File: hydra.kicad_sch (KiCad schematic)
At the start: 59 parts, among them J1 PC104 Interconnect, J2 STLINK/V2 Header, J3 STLINK/V2 Clone Header, J4 USB Conn, J5 UART Header, U2 AMS1117-3.3, U3 STM32F103VCTx, Y1 16mHz

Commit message: feat: mostly done pcb
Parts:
- removed D2: Power LED, symbol Device:LED
- removed J4: USB Conn, symbol Connector:USB_C_Receptacle_USB2.0_14P
- removed R2, R3, R4: 5.1k, symbol Device:R
- removed R5: 9k, symbol Device:R
- added C10, C11, C12, C13, C14: 0.1uF, Capacitor_SMD:C_0603_1608Metric, symbol Device:C
- added H1, H2, H3, H4: MountingHole, MountingHole:MountingHole_3.2mm_M3_DIN965_Pad, symbol Mechanical:MountingHole
- C1, C2, C3, C4, C5, C6, C7, C8, C9: footprint (none) -> Capacitor_SMD:C_0603_1608Metric
- D1, D10, D11, D12, D13, D14, D3, D4, D5, D6, D7, D8, D9: footprint (none) -> LED_SMD:LED_0603_1608Metric
- J1: footprint (none) -> Connector_PinHeader_2.54mm:PinHeader_2x32_P2.54mm_Vertical; symbol Connector_Generic_MountingPin:Conn_02x32_Row_Letter_First_MountingPin -> Connector_Generic_MountingPin:Conn_02x32_Odd_Even_MountingPin
- J2: footprint (none) -> Connector_PinHeader_2.54mm:PinHeader_2x10_P2.54mm_Vertical
- J3: footprint (none) -> Connector_PinHeader_2.54mm:PinHeader_2x05_P2.54mm_Vertical
- J5: footprint (none) -> Connector_PinHeader_2.54mm:PinHeader_1x03_P2.54mm_Vertical
- R1: value 4.7k -> 5.1k; footprint (none) -> Resistor_SMD:R_0603_1608Metric
- R10, R11, R12, R13, R14, R15, R16, R6, R7, R8, R9: value 4.7K -> 5.1K; footprint (none) -> Resistor_SMD:R_0603_1608Metric
- R17: value 4.7K -> 5.1K; footprint (none) -> Capacitor_SMD:C_0603_1608Metric
- TP1, TP10, TP11, TP2, TP3, TP4, TP5, TP6, TP7, TP8, TP9: footprint (none) -> TestPoint:TestPoint_Pad_D1.0mm
- Y1: footprint (none) -> Crystal:Crystal_HC49-U_Vertical
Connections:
- net +3V3: now also C10.1, C11.1, C12.1, C13.1, C14.1
- net 3V3_CONN: now also J1.57 (Pin_57), J1.58 (Pin_58); no longer J1.a29 (Pin_a29), J1.b29 (Pin_b29)
- net CS_1: now also J1.1 (Pin_1), J1.2 (Pin_2), U3.67 (PA8); no longer J1.a1 (Pin_a1), J1.b1 (Pin_b1), U3.15 (PC0)
- net CS_10: now also J1.19 (Pin_19), J1.20 (Pin_20), U3.58 (PD11); no longer J1.a10 (Pin_a10), J1.b10 (Pin_b10), U3.66 (PC9)
- net CS_11: now also J1.21 (Pin_21), J1.22 (Pin_22), U3.57 (PD10); no longer J1.a11 (Pin_a11), J1.b11 (Pin_b11), U3.78 (PC10)
- net CS_12: now also J1.23 (Pin_23), J1.24 (Pin_24), U3.56 (PD9); no longer J1.a12 (Pin_a12), J1.b12 (Pin_b12), U3.79 (PC11)
- net CS_2: now also J1.3 (Pin_3), J1.4 (Pin_4), U3.66 (PC9); no longer J1.a2 (Pin_a2), J1.b2 (Pin_b2), U3.16 (PC1)
- net CS_3: now also J1.5 (Pin_5), J1.6 (Pin_6), U3.65 (PC8); no longer J1.a3 (Pin_a3), J1.b3 (Pin_b3), U3.17 (PC2)
- net CS_4: now also J1.7 (Pin_7), J1.8 (Pin_8), U3.64 (PC7); no longer J1.a4 (Pin_a4), J1.b4 (Pin_b4), U3.18 (PC3)
- net CS_5: now also J1.10 (Pin_10), J1.9 (Pin_9), U3.63 (PC6); no longer J1.a5 (Pin_a5), J1.b5 (Pin_b5), U3.33 (PC4)
- net CS_6: now also J1.11 (Pin_11), J1.12 (Pin_12), U3.62 (PD15); no longer J1.a6 (Pin_a6), J1.b6 (Pin_b6), U3.34 (PC5)
- net CS_7: now also J1.13 (Pin_13), J1.14 (Pin_14), U3.61 (PD14); no longer J1.a7 (Pin_a7), J1.b7 (Pin_b7), U3.63 (PC6)
- net CS_8: now also J1.15 (Pin_15), J1.16 (Pin_16), U3.60 (PD13); no longer J1.a8 (Pin_a8), J1.b8 (Pin_b8), U3.64 (PC7)
- net CS_9: now also J1.17 (Pin_17), J1.18 (Pin_18), U3.59 (PD12); no longer J1.a9 (Pin_a9), J1.b9 (Pin_b9), U3.65 (PC8)
- net GND: now also J1.63 (Pin_63), J1.64 (Pin_64), C10.2, C11.2, C12.2, C13.2, C14.2; no longer J1.a32 (Pin_a32), J1.b32 (Pin_b32)
- net P_MISO: now also J1.26 (Pin_26); no longer J1.b13 (Pin_b13)
- net P_MOSI: now also J1.25 (Pin_25); no longer J1.a13 (Pin_a13)
- net P_SCLK: now also J1.27 (Pin_27); no longer J1.a14 (Pin_a14)
- net R_CS: now also J1.31 (Pin_31), U3.55 (PD8); no longer J1.a16 (Pin_a16)
- net R_MOSI: now also J1.33 (Pin_33); no longer J1.a17 (Pin_a17), TP10.1
- net SWIM: now also J2.11 (Pin_11)
- net S_MISO: now also J1.30 (Pin_30); no longer J1.b15 (Pin_b15)
- net S_MOSI: now also J1.29 (Pin_29); no longer J1.a15 (Pin_a15)
- net S_SCLK: now also J1.28 (Pin_28); no longer J1.b14 (Pin_b14)
- net USART_RX: now also J5.1 (Pin_1); no longer J5.2 (Pin_2)
- net USART_TX: now also J5.2 (Pin_2); no longer J5.1 (Pin_1)
- net OSC-: now reaches C8.2, U3.13 (OSC_OUT), Y1.1
- net OSC+: now reaches C7.2, U3.12 (OSC_IN), Y1.2
- removed net +5V: J1.a28 (Pin_a28), J1.b28 (Pin_b28)
- net JTDO renamed JTDO/R_SCLK
- net JTDO/R_SCLK: now also J1.32 (Pin_32); no longer J1.b16 (Pin_b16)
- net NJTRST renamed NJTRST/R_MISO
- net NJTRST/R_MISO: now also J1.34 (Pin_34), TP10.1; no longer J1.b17 (Pin_b17)
- net USB_D+: no longer names the net of U3.71 (PA12)
- net USB_D-: no longer names the net of U3.70 (PA11)
- net USB_VBUS: no longer names the net of U3.80 (PC12)
- no-connect marks 81 -> 84
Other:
- note removed: "USB"
- moved on the sheet: C1, C2, C3, C4, C5, C6, C7, C8, C9, D1, D10, D11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

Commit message: feat: trying multinodal
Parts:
- removed C10, C11, C12, C13, C14, C4, C5, C6, C9: 0.1uF, Capacitor_SMD:C_0603_1608Metric, symbol Device:C
- removed C7, C8: 20pF, Capacitor_SMD:C_0603_1608Metric, symbol Device:C
- removed J2: STLINK/V2 Header, Connector_PinHeader_2.54mm:PinHeader_2x10_P2.54mm_Vertical, symbol Connector_Generic:Conn_02x10_Odd_Even
- removed J3: STLINK/V2 Clone Header, Connector_PinHeader_2.54mm:PinHeader_2x05_P2.54mm_Vertical, symbol Connector_Generic:Conn_02x05_Top_Bottom
- removed J5: UART Header, Connector_PinHeader_2.54mm:PinHeader_1x03_P2.54mm_Vertical, symbol Connector:Conn_01x03_Pin
- removed TP2: Reset_TP, TestPoint:TestPoint_Pad_D1.0mm, symbol Connector:TestPoint
- removed U3: STM32F103VCTx, Package_QFP:LQFP-100_14x14mm_P0.5mm, symbol MCU_ST_STM32F1:STM32F103VCTx
- removed Y1: 16mHz, Crystal:Crystal_HC49-U_Vertical, symbol Device:Crystal
- added J1: UART Header, Connector_PinHeader_2.54mm:PinHeader_1x03_P2.54mm_Vertical, symbol Connector:Conn_01x03_Pin
- renumbered C3 to C1, C1 to C2, C2 to C3, D11 to D10, D12 to D11, D13 to D12, D14 to D13, D3 to D2, D4 to D3, D5 to D4, D6 to D5, D7 to D6, D8 to D7, D9 to D8, D10 to D9, H3 to H2, H2 to H3, J1 to J2, R14 to R10, R15 to R11, R16 to R12, R17 to R13, R6 to R2, R7 to R3, R8 to R4, R9 to R5, R10 to R6, R11 to R7, R12 to R8, R13 to R9, TP11 to TP10, TP3 to TP2, TP4 to TP3, TP5 to TP4, TP6 to TP5, TP7 to TP6, TP8 to TP7, TP9 to TP8, TP10 to TP9, U2 to U1
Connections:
- net GND: now also J1.3 (Pin_3)
- net USART_RX: now also J1.1 (Pin_1)
- net USART_TX: now also J1.2 (Pin_2)
- net JTDO/R_SCLK renamed R_SCLK
- net NJTRST/R_MISO renamed R_MISO
- no-connect marks 84 -> 37
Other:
- added sheet Node (node.kicad_sch)
- added sheet Node1 (node.kicad_sch)
- added sheet Node2 (node.kicad_sch)
- added sheet Node3 (node.kicad_sch)
- added sheet Node4 (node.kicad_sch)
- note added: "Nodes"
- note removed: "MCU"
- moved on the sheet: C1, D10, D11, D12, D13, D2, D3, D4, D5, D6, D7, D8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

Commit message: feat: in progress rework
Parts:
- removed C1: 4.7uF, Capacitor_SMD:C_0603_1608Metric, symbol Device:C
- removed D10: CS9, LED_SMD:LED_0603_1608Metric, symbol Device:LED
- removed D11: CS10, LED_SMD:LED_0603_1608Metric, symbol Device:LED
- removed D12: CS11, LED_SMD:LED_0603_1608Metric, symbol Device:LED
- removed D13: CS12, LED_SMD:LED_0603_1608Metric, symbol Device:LED
- removed D2: CS1, LED_SMD:LED_0603_1608Metric, symbol Device:LED
- removed D3: CS2, LED_SMD:LED_0603_1608Metric, symbol Device:LED
- removed D4: CS3, LED_SMD:LED_0603_1608Metric, symbol Device:LED
- removed D5: CS4, LED_SMD:LED_0603_1608Metric, symbol Device:LED
- removed D6: CS5, LED_SMD:LED_0603_1608Metric, symbol Device:LED
- removed D7: CS6, LED_SMD:LED_0603_1608Metric, symbol Device:LED
- removed D8: CS7, LED_SMD:LED_0603_1608Metric, symbol Device:LED
- removed D9: CS8, LED_SMD:LED_0603_1608Metric, symbol Device:LED
- removed J1: UART Header, Connector_PinHeader_2.54mm:PinHeader_1x03_P2.54mm_Vertical, symbol Connector:Conn_01x03_Pin
- removed R10, R11, R12, R2, R3, R4, R5, R6, R7, R8, R9: 5.1K, Resistor_SMD:R_0603_1608Metric, symbol Device:R
- removed R13: 5.1K, Capacitor_SMD:C_0603_1608Metric, symbol Device:R
- added R24, R25: R, symbol Device:R
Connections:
- net +3V3: now also R24.1, R25.1
- net INTRA_SCL: now also R24.2
- net INTRA_SDA: now also R25.2
- no-connect marks 37 -> 27
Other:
- removed sheet Node1
- removed sheet Node2
- removed sheet Node3
- removed sheet Node4
- sheet Node ports: added none; removed JTDO, NJTRST, USART_RX, USART_TX
- note added: "Keep this empty. More nodes will eventually go here."
- note added: "Max: 1A"
- moved on the sheet: H1, H2, H3, H4

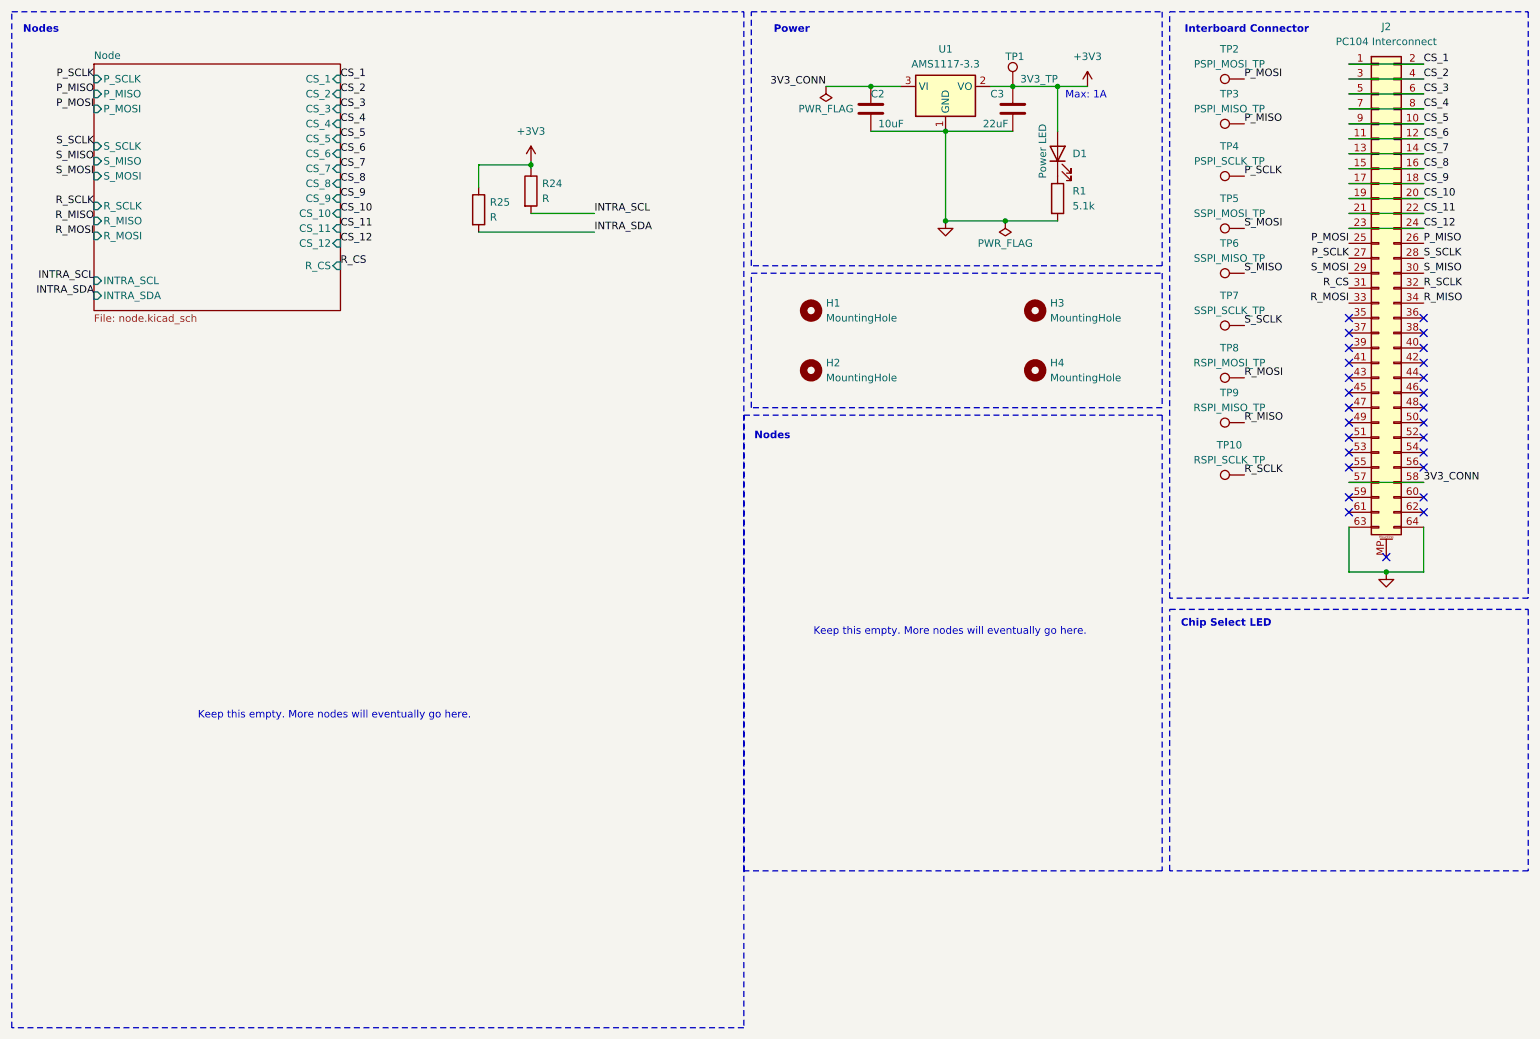
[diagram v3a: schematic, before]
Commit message: feat: trying out a diff mcu
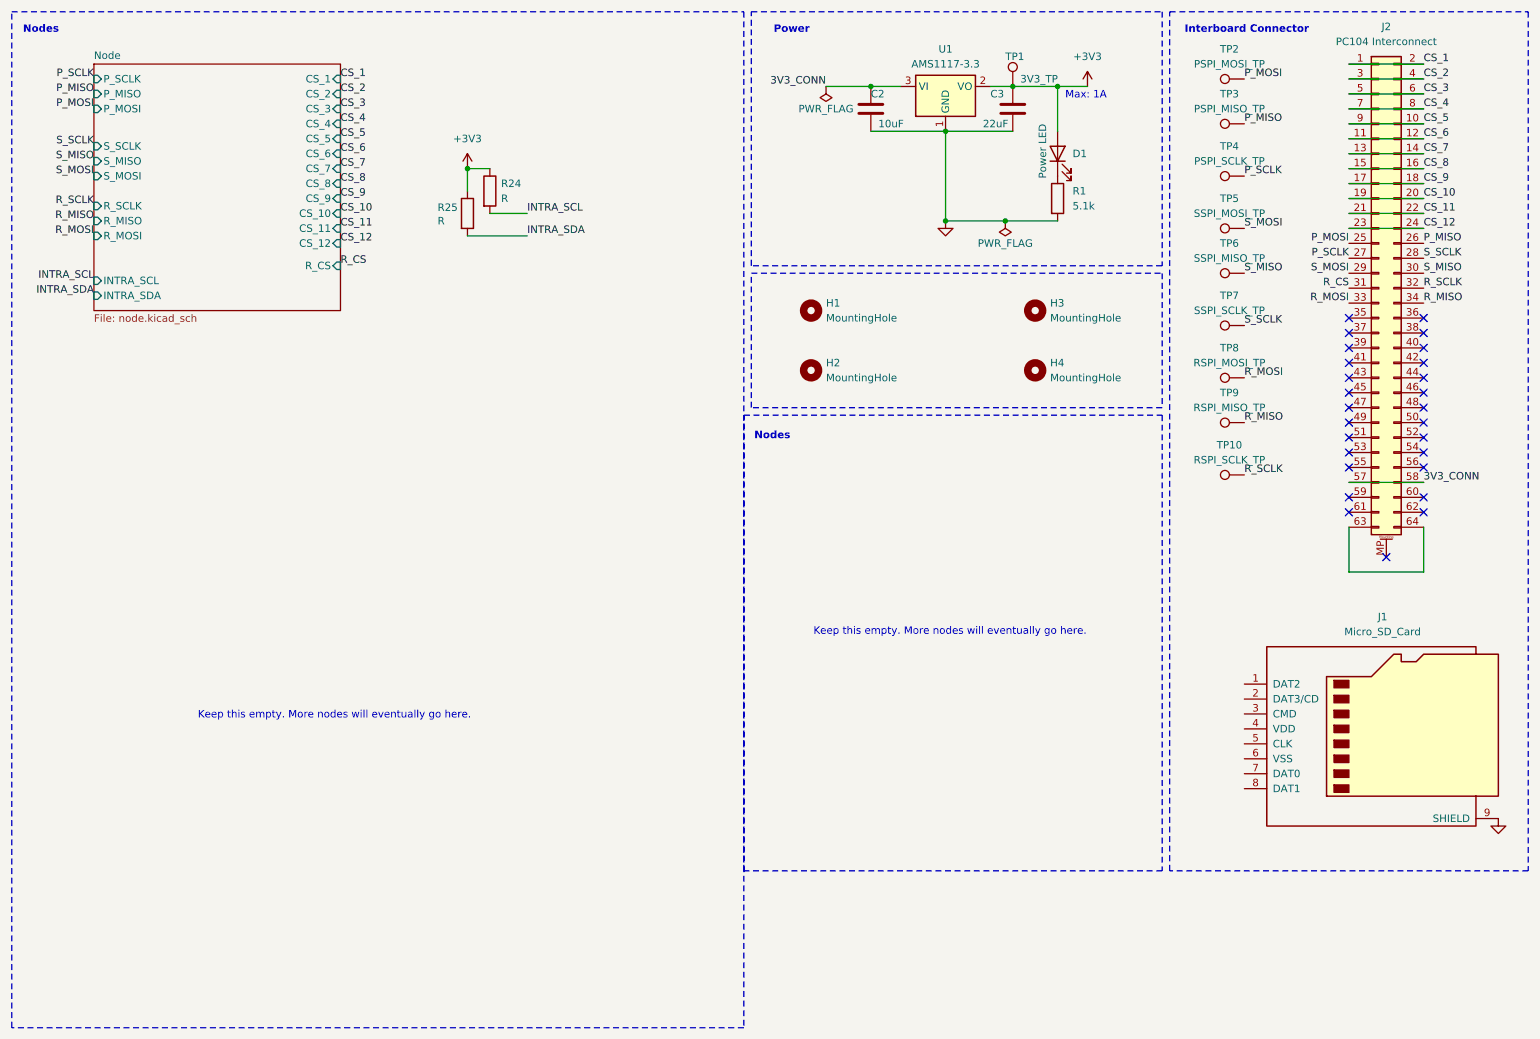
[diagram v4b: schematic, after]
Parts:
- added J1: Micro_SD_Card, symbol Connector:Micro_SD_Card
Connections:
- net GND: now also J1.9 (SHIELD); no longer J2.63 (Pin_63), J2.64 (Pin_64)
- new net: J2.63 (Pin_63), J2.64 (Pin_64)
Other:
- note removed: "Chip Select LED"
- moved on the sheet: R24, R25
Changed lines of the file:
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@@
-	)
-	(junction
-		(at 109.855 42.545)
-		(diameter 0)
-		(color 0 0 0 0)
-	)
-	(junction
-		(at 255.27 111.76)
-		(diameter 0)
-		(color 0 0 0 0)
 	)
 	(junction
@@
 	)
 	(junction
+		(at 99.06 43.18)
+		(diameter 0)
+		(color 0 0 0 0)
+	)
+	(junction
 		(at 190.5 52.07)
 		(diameter 0)
@@
 	(wire
 		(pts
+			(xy 102.87 50.8) (xy 109.22 50.8)
+		)
+		(stroke
+			(width 0)
+			(type default)
+		)
+	)
+	(wire
+		(pts
 			(xy 248.92 96.52) (xy 261.62 96.52)
 		)
@@
 	(wire
 		(pts
-			(xy 109.855 42.545) (xy 100.965 42.545)
-		)
-		(stroke
-			(width 0)
-			(type default)
-		)
-	)
-	(wire
-		(pts
-			(xy 109.855 50.8) (xy 120.65 50.8)
-		)
-		(stroke
-			(width 0)
-			(type default)
-		)
-	)
-	(wire
-		(pts
 			(xy 248.92 27.94) (xy 261.62 27.94)
 		)
@@
 	(wire
 		(pts
-			(xy 100.965 42.545) (xy 100.965 46.355)
+			(xy 99.06 43.18) (xy 99.06 46.99)
 		)
 		(stroke
@@
 	(wire
 		(pts
-			(xy 248.92 111.76) (xy 255.27 111.76)
+			(xy 248.92 111.76) (xy 261.62 111.76)
 		)
 		(stroke
@@
 	(wire
 		(pts
-			(xy 100.965 53.975) (xy 120.65 53.975)
-		)
-		(stroke
-			(width 0)
-			(type default)
-		)
-	)
-	(wire
-		(pts
-			(xy 255.27 111.76) (xy 261.62 111.76)
-		)
-		(stroke
-			(width 0)
-			(type default)
-		)
-	)
-	(wire
-		(pts
-			(xy 109.855 41.91) (xy 109.855 42.545)
-		)
-		(stroke
-			(width 0)
-			(type default)
-		)
-	)
-	(wire
-		(pts
 			(xy 199.39 29.21) (xy 199.39 36.83)
 		)
@@
 	(wire
 		(pts
-			(xy 109.855 42.545) (xy 109.855 43.18)
+			(xy 99.06 54.61) (xy 109.22 54.61)
 		)
 		(stroke
@@
 		(pts
 			(xy 160.02 29.21) (xy 167.64 29.21)
+		)
+		(stroke
+			(width 0)
+			(type default)
+		)
+	)
+	(wire
+		(pts
+			(xy 99.06 43.18) (xy 102.87 43.18)
 		)
 		(stroke
@@
 	(rectangle
 		(start 218.44 16.51)
-		(end 279.4 116.205)
+		(end 279.4 162.56)
 		(stroke
 			(width 0)
@@
 	)
 	(rectangle
-		(start 218.44 118.11)
-		(end 279.4 162.56)
-		(stroke
-			(width 0)
-			(type dash)
-		)
-		(fill
-			(type none)
-		)
-	)
-	(rectangle
 		(start 21.59 16.51)
 		(end 146.05 189.23)
@@
 		)
 	)
-	(text "Chip Select LED"
-		(exclude_from_sim no)
-		(at 220.345 121.285 0)
+	(text "Keep this empty. More nodes will eventually go here."
+		(exclude_from_sim no)
+		(at 76.454 136.144 0)
+		(effects
+			(font
+				(size 1.27 1.27)
+			)
+		)
+	)
+	(text "Power"
+		(exclude_from_sim no)
+		(at 151.13 20.32 0)
 		(effects
 			(font
@@
 		)
 	)
-	(text "Keep this empty. More nodes will eventually go here."
-		(exclude_from_sim no)
-		(at 76.454 136.144 0)
-		(effects
-			(font
-				(size 1.27 1.27)
-			)
-		)
-	)
-	(text "Power"
-		(exclude_from_sim no)
-		(at 151.13 20.32 0)
+	(text "Nodes"
+		(exclude_from_sim no)
+		(at 147.828 89.408 0)
 		(effects
 			(font
@@
 		)
 	)
-	(text "Nodes"
-		(exclude_from_sim no)
-		(at 147.828 89.408 0)
-		(effects
-			(font
-				(size 1.27 1.27)
-				(thickness 0.254)
-				(bold yes)
-			)
-			(justify left bottom)
-		)
-	)
 	(label "CS_7"
 		(at 77.47 43.18 0)
@@
 	)
 	(label "INTRA_SDA"
-		(at 120.65 53.975 0)
+		(at 109.22 54.61 0)
 		(fields_autoplaced yes)
 		(effects
@@
 	)
 	(label "INTRA_SCL"
-		(at 120.65 50.8 0)
+		(at 109.22 50.8 0)
 		(fields_autoplaced yes)
 		(effects
@@
 	(symbol
 		(lib_id "power:+3V3")
-		(at 109.855 41.91 0)
+		(at 99.06 43.18 0)
 		(unit 1)
 		(exclude_from_sim no)
@@
 		(fields_autoplaced yes)
 		(property "Reference" "#PWR053"
-			(at 109.855 45.72 0)
+			(at 99.06 46.99 0)
 			(effects
 				(font
@@
 		)
 		(property "Value" "+3V3"
-			(at 109.855 36.83 0)
+			(at 99.06 38.1 0)
 			(effects
 				(font
@@
 		)
 		(property "Footprint" ""
-			(at 109.855 41.91 0)
+			(at 99.06 43.18 0)
 			(effects
 				(font
@@
 		)
 		(property "Datasheet" ""
-			(at 109.855 41.91 0)
+			(at 99.06 43.18 0)
 			(effects
 				(font
@@
 		)
 		(property "Description" ""
-			(at 109.855 41.91 0)
+			(at 99.06 43.18 0)
 			(effects
 				(font
@@
 	)
 	(symbol
+		(lib_id "Connector:Micro_SD_Card")
+		(at 254 138.43 0)
+		(unit 1)
+		(exclude_from_sim no)
+		(in_bom yes)
+		(on_board yes)
+		(dnp no)
+		(fields_autoplaced yes)
+		(property "Reference" "J1"
+			(at 254.635 119.38 0)
+			(effects
+				(font
+					(size 1.27 1.27)
+				)
+			)
+		)
+		(property "Value" "Micro_SD_Card"
+			(at 254.635 121.92 0)
+			(effects
+				(font
+					(size 1.27 1.27)
+				)
+			)
+		)
+		(property "Footprint" ""
+			(at 283.21 130.81 0)
+			(effects
+				(font
+					(size 1.27 1.27)
+				)
+				(hide yes)
+			)
+		)
+		(property "Datasheet" "http://katalog.we-online.de/em/datasheet/693072010801.pdf"
+			(at 254 138.43 0)
+			(effects
+				(font
+					(size 1.27 1.27)
+				)
+				(hide yes)
+			)
+		)
+		(property "Description" "Micro SD Card Socket"
+			(at 254 138.43 0)
+			(effects
+				(font
+					(size 1.27 1.27)
+				)
+				(hide yes)
+			)
+		)
+		(pin "9"
+		)
+		(pin "4"
+		)
+		(pin "8"
+		)
+		(pin "7"
+		)
+		(pin "6"
+		)
+		(pin "5"
+		)
+		(pin "1"
+		)
+		(pin "3"
+		)
+		(pin "2"
+		)
+		(instances
+			(project "hydra"
+				(path "/0756f948-9f90-462f-bcf0-9b6a1e04b393"
+					(reference "J1")
+					(unit 1)
+				)
+			)
+		)
+	)
+	(symbol
 		(lib_id "Mechanical:MountingHole")
 		(at 157.48 77.47 0)
@@
 	(symbol
 		(lib_id "Device:R")
-		(at 109.855 46.99 0)
+		(at 102.87 46.99 0)
 		(unit 1)
 		(exclude_from_sim no)
@@
 		(dnp no)
 		(property "Reference" "R24"
-			(at 111.76 45.72 0)
+			(at 104.775 45.72 0)
 			(effects
 				(font
@@
 		)
 		(property "Value" "R"
-			(at 111.76 48.26 0)
+			(at 104.775 48.26 0)
 			(effects
 				(font
@@
 		)
 		(property "Footprint" ""
-			(at 108.077 46.99 90)
+			(at 101.092 46.99 90)
 			(effects
 				(font
@@
 		)
 		(property "Datasheet" "~"
-			(at 109.855 46.99 0)
+			(at 102.87 46.99 0)
 			(effects
 				(font
@@
 		)
 		(property "Description" ""
-			(at 109.855 46.99 0)
+			(at 102.87 46.99 0)
 			(effects
 				(font
@@
 	(symbol
 		(lib_id "power:GND")
-		(at 255.27 111.76 0)
+		(at 274.32 153.67 0)
 		(unit 1)
 		(exclude_from_sim no)
@@
 		(dnp no)
 		(property "Reference" "#PWR06"
-			(at 255.27 118.11 0)
+			(at 274.32 160.02 0)
 			(effects
 				(font
@@
 		)
 		(property "Value" "GND"
-			(at 259.08 113.03 0)
+			(at 278.13 154.94 0)
 			(effects
 				(font
@@
 		)
 		(property "Footprint" ""
-			(at 255.27 111.76 0)
+			(at 274.32 153.67 0)
 			(effects
 				(font
@@
 		)
 		(property "Datasheet" ""
-			(at 255.27 111.76 0)
+			(at 274.32 153.67 0)
 			(effects
 				(font
@@
 		)
 		(property "Description" ""
-			(at 255.27 111.76 0)
+			(at 274.32 153.67 0)
 			(effects
 				(font
@@
 	(symbol
 		(lib_id "Device:R")
-		(at 100.965 50.165 0)
+		(at 99.06 50.8 0)
 		(unit 1)
 		(exclude_from_sim no)
@@
 		(dnp no)
 		(property "Reference" "R25"
-			(at 102.87 48.895 0)
+			(at 93.98 49.784 0)
 			(effects
 				(font
@@
 		)
 		(property "Value" "R"
-			(at 102.87 51.435 0)
+			(at 93.98 52.07 0)
 			(effects
 				(font
@@
 		)
 		(property "Footprint" ""
-			(at 99.187 50.165 90)
+			(at 97.282 50.8 90)
 			(effects
 				(font
@@
 		)
 		(property "Datasheet" "~"
-			(at 100.965 50.165 0)
+			(at 99.06 50.8 0)
 			(effects
 				(font
@@
 		)
 		(property "Description" ""
-			(at 100.965 50.165 0)
-			(effects
-				(font
+			(at 99.06 50.8 0)
+			(effects
+				(font
